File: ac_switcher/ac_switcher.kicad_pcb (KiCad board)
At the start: 2 copper layers, 32.5 x 28.4 mm, 16 parts, among them U1 MOC3061M, U2 BTB600

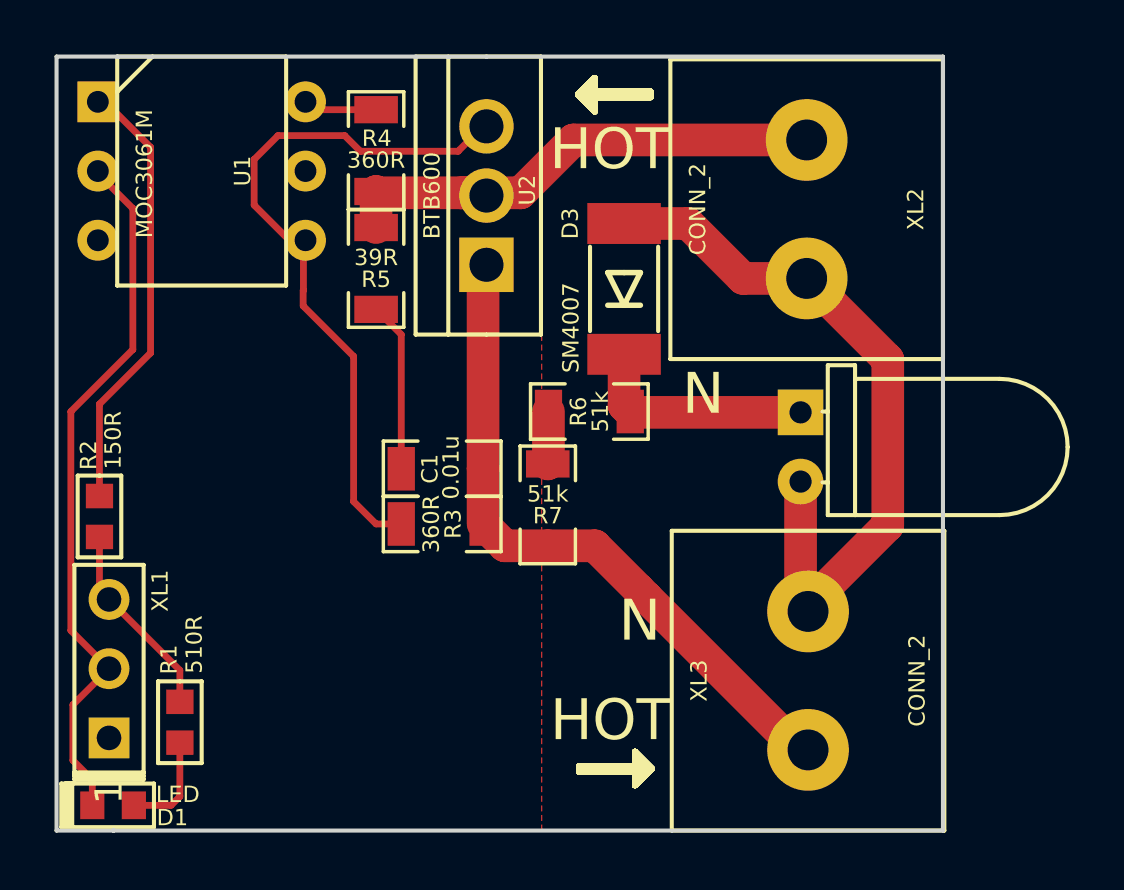
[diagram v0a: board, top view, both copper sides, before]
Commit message: + Add ac switcher gerber files.
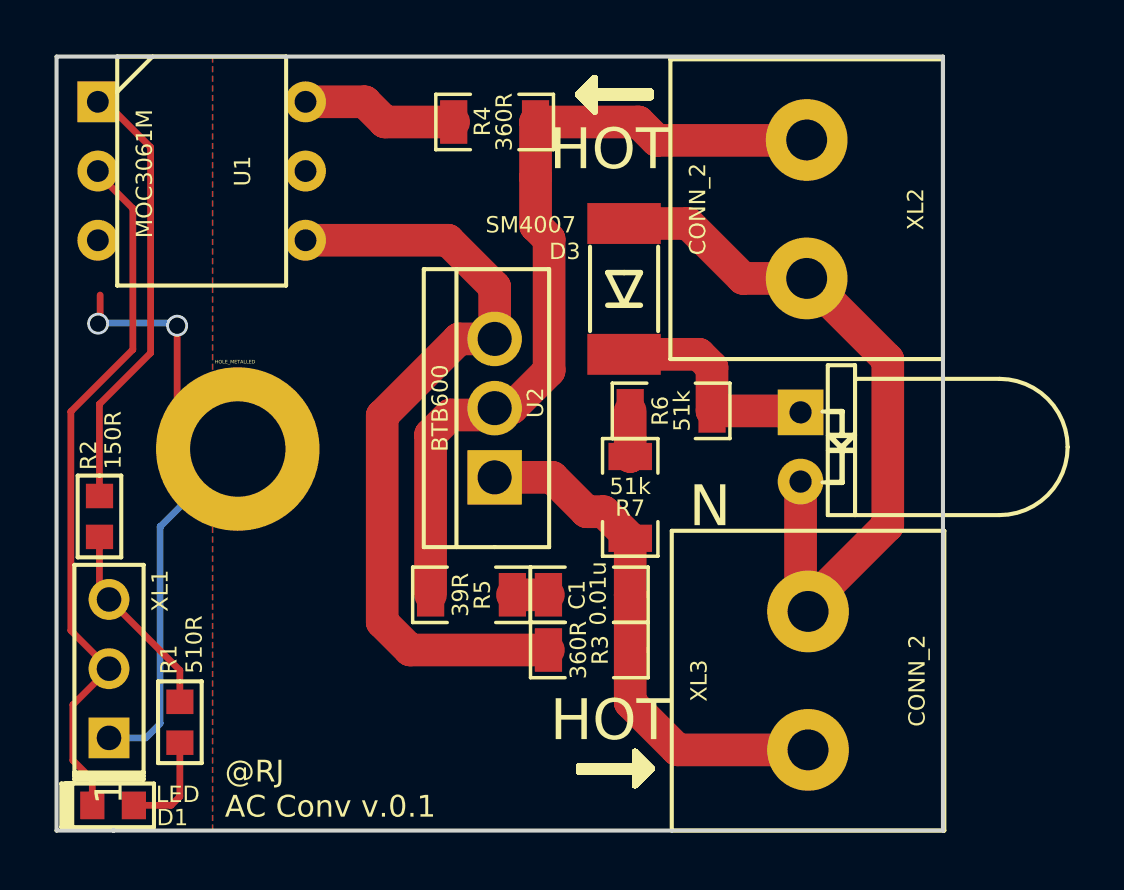
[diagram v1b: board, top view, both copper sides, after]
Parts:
- added HOLE1: HOLE_METALLED, PCB:Hole3_5_out6mm, F.Cu at (144.4, 76.8)
- moved R5 12.5 mm to (153.0, 82.2), turned to 0 degrees
- moved U2 7.81 mm to (153.8, 75.3)
- moved C1 7.11 mm to (157.3, 82.2)
- moved R3 7.11 mm to (157.3, 84.2)
- moved R4 4.47 mm to (153.8, 64.8), turned to 180 degrees
- moved R7 3.04 mm to (158.8, 78.6)
- moved R6 3.00 mm to (160.3, 75.4)
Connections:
- net Net-(C1-Pad1) renamed /AC_FILT
- net Net-(R3-Pad1) renamed /AC2
- net Net-(R4-Pad2) renamed /AC1
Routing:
- net GND: track 0.00 -> 23.5 mm, vias 0 -> 2
- net /HOT_IN: track 18.9 -> 30.8 mm
- net /HOT_OUT: track 25.3 -> 20.0 mm
- net /AC_FILT: track 6.23 -> 1.32 mm
- net /AC1: track 2.71 -> 6.15 mm
- net /AC2: track 26.3 -> 29.5 mm
- net /D1: track 9.04 -> 8.35 mm
- added copper zone on B.Cu, net GND
- added copper zone on F.Cu, net GND
- removed copper zone on F.Cu, net /NEUTRAL
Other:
- board text added: "@RJ AC Conv v.0.1"
